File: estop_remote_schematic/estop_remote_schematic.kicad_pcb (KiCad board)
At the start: 2 copper layers, 60 x 75 mm, 22 parts, among them J1 Power Switch, J2 ESP32 Pins 1-22, J3 ESP32 Pins 23-44, J4 Battery Connector, J5 EStop Button, J6 OLed Screen Pins, J7 HC12 Connections, J8 Reset Button, J9 RotaryEnc Connections

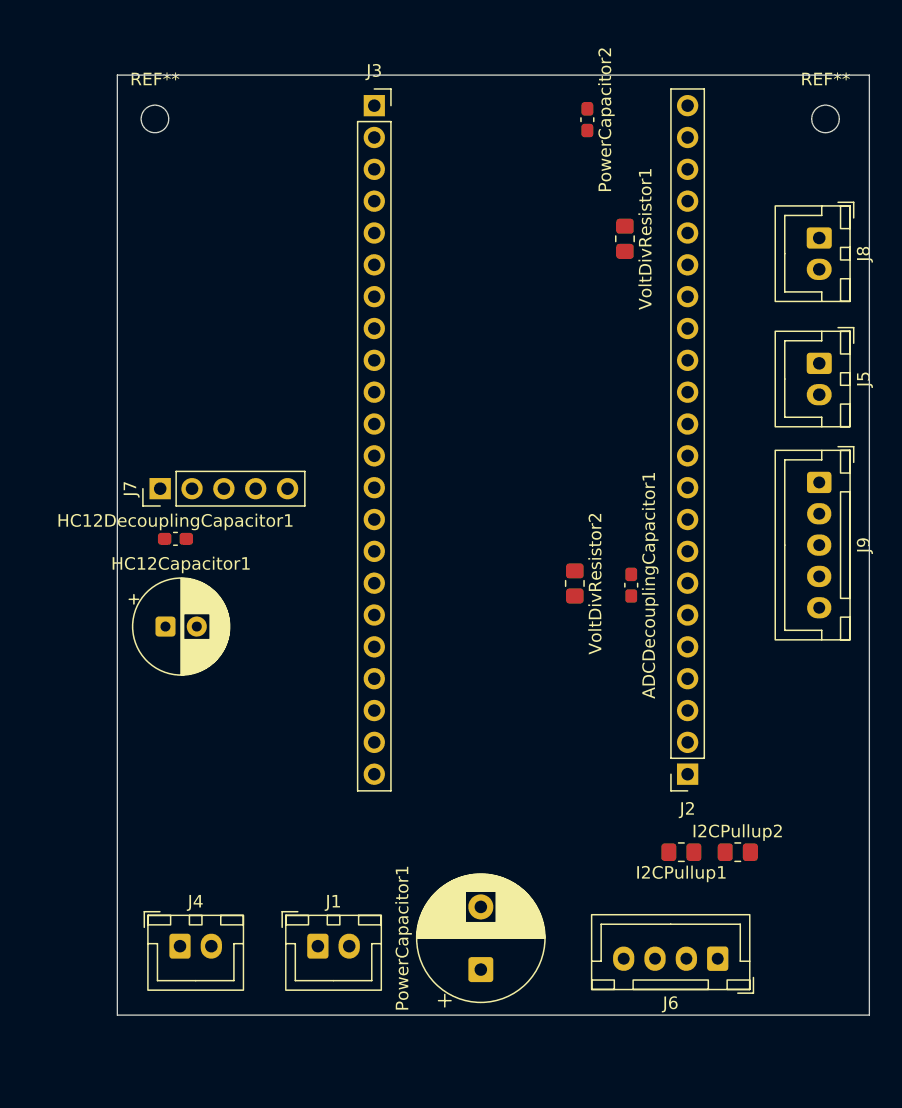
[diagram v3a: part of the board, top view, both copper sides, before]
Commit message: Added preliminary traces; connected all components and is ready for rule checks and ground plane
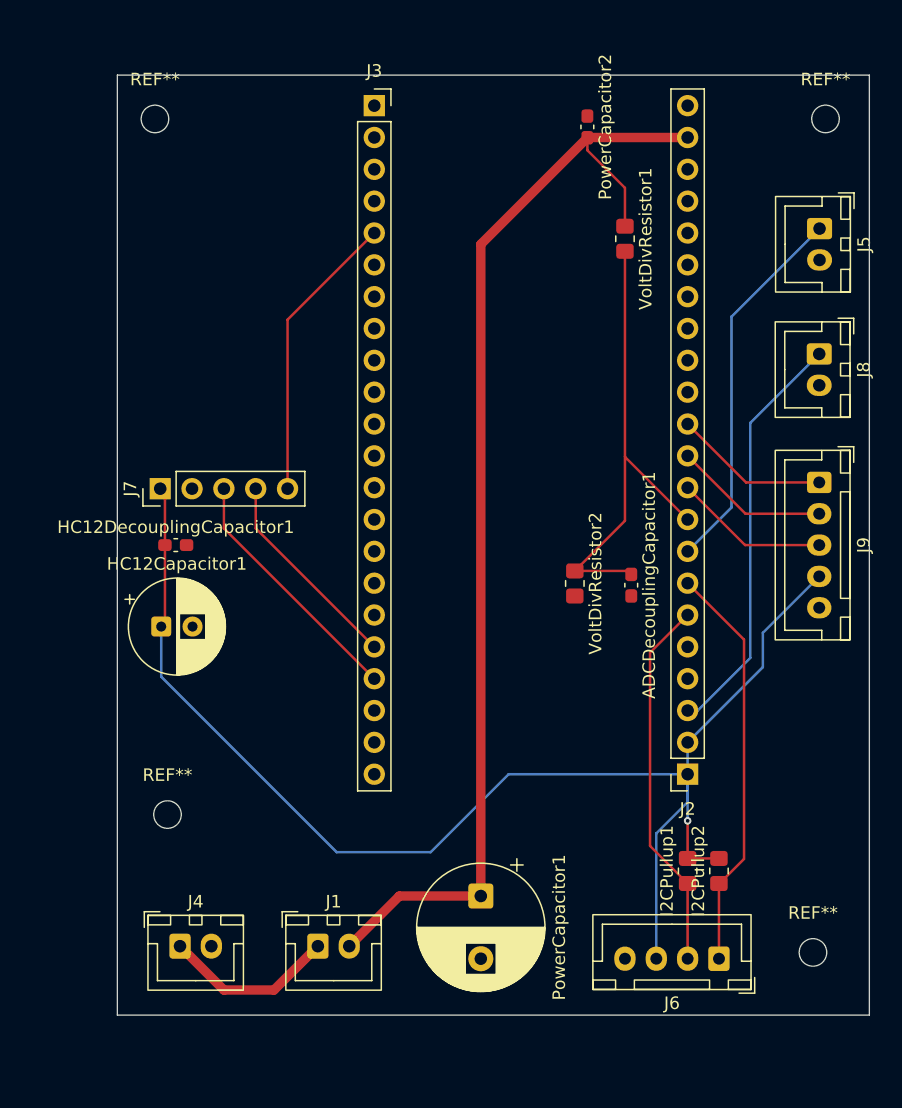
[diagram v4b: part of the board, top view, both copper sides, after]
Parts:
- added REF**: MountingHole_2.2mm_M2, MountingHole:MountingHole_2.2mm_M2, F.Cu at (123.5, 102.0)
- added REF**: MountingHole_2.2mm_M2, MountingHole:MountingHole_2.2mm_M2, F.Cu at (72.0, 91.0)
- moved J5 10.8 mm to (124.0, 44.2)
- moved J8 9.25 mm to (124.0, 54.2)
- moved PowerCapacitor1 5.87 mm to (97.0, 97.5), turned to -90 degrees
- moved I2CPullup2 2.12 mm to (116.0, 95.5), turned to 90 degrees
- moved I2CPullup1 1.58 mm to (113.5, 95.5), turned to 90 degrees
- moved PowerCapacitor2 0.58 mm to (105.5, 36.1)
- moved HC12DecouplingCapacitor1 0.50 mm to (72.7, 69.5)
- moved HC12Capacitor1 0.34 mm to (71.5, 76.0)
- moved J6 0.10 mm to (116.0, 102.5)
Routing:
- net +3.3V: track 0.00 -> 110.8 mm, vias 0 -> 1
- net +6V: track 0.00 -> 92.5 mm
- net /BatteryVoltageDivider: track 0.00 -> 38.8 mm
- net /Reset: track 0.00 -> 33.3 mm
- net /SDA: track 0.00 -> 32.7 mm
- net /EStopSignal: track 0.00 -> 30.1 mm
- net /SCL: track 0.00 -> 29.9 mm
- net /HC12_SET: track 0.00 -> 23.3 mm
- net /HC12_RX: track 0.00 -> 20.1 mm
- net /HC12_TX: track 0.00 -> 16.5 mm
- net Net-(J1-Pin_1): track 0.00 -> 13.9 mm
- net /ChannelEncoderB: track 0.00 -> 12.4 mm
- net /ChannelEncoderA: track 0.00 -> 12.4 mm
- net /ChannelEncoderSignal: track 0.00 -> 12.4 mm

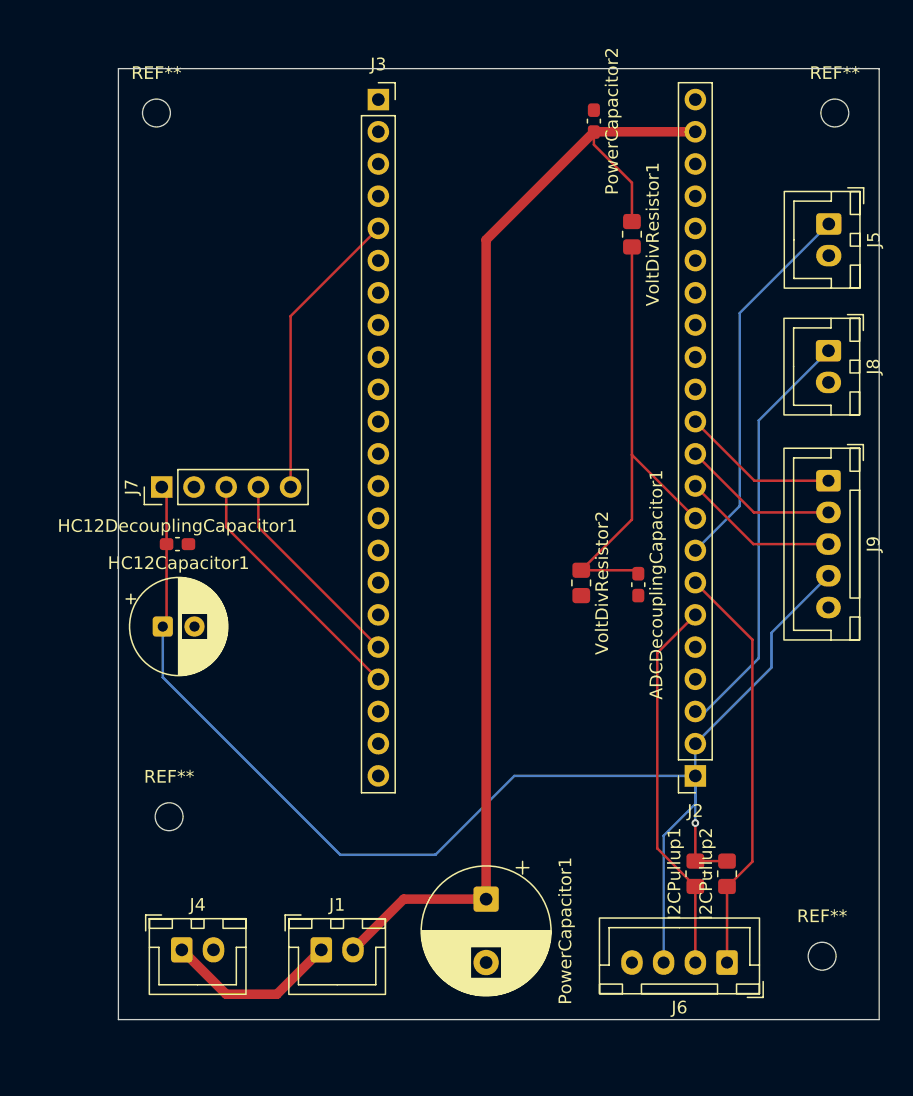
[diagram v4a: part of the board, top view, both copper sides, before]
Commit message: Poured ground plane on layer B.cu, added dog bone vias for SMT components
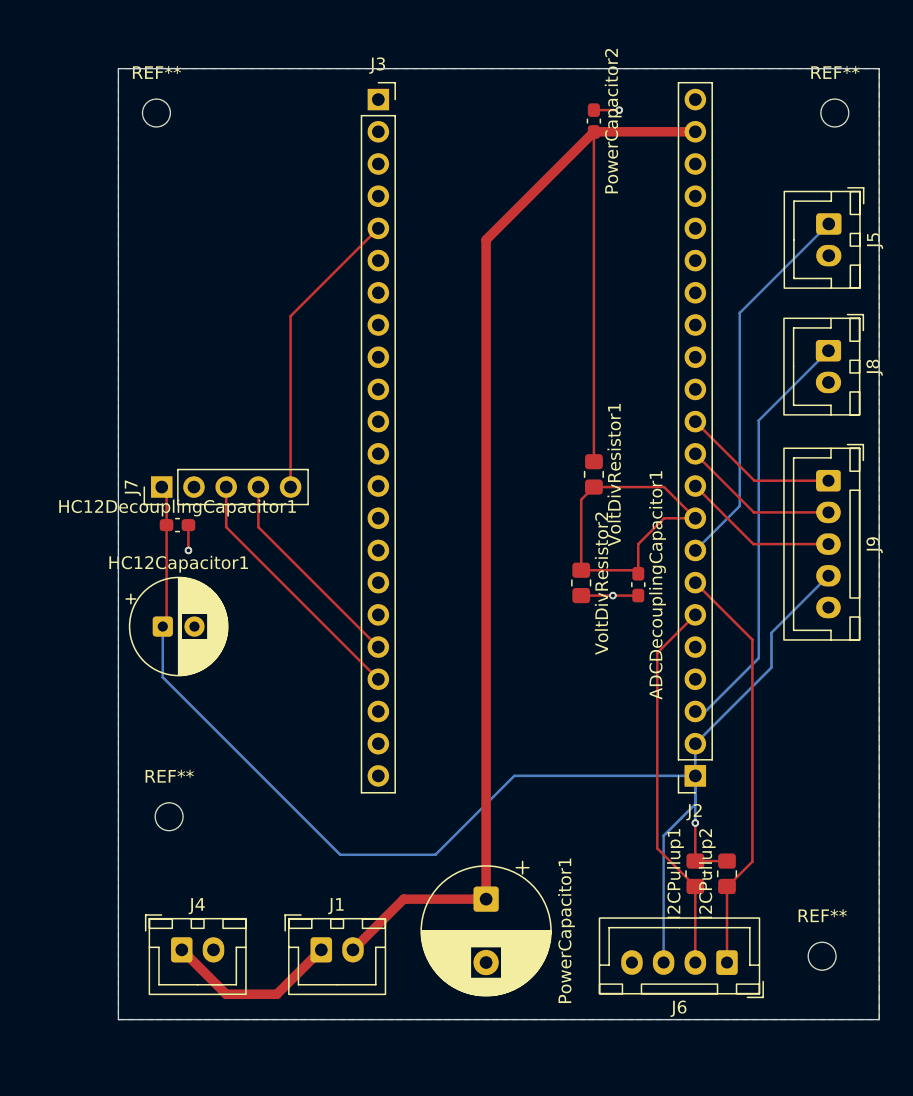
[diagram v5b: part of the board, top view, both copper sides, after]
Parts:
- moved VoltDivResistor1 19.2 mm to (105.5, 64.0)
- moved HC12DecouplingCapacitor1 1.50 mm to (72.7, 68.0)
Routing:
- net +6V: track 92.5 -> 110.2 mm
- net /BatteryVoltageDivider: track 38.8 -> 28.3 mm
- net GND: track 0.00 -> 8.50 mm, vias 0 -> 3
- added copper zone on B.Cu, net GND
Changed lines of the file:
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@@
 	(footprint "Resistor_SMD:R_0805_2012Metric_Pad1.20x1.40mm_HandSolder"
 		(layer "F.Cu")
-		(at 108.5 45.06 -90)
+		(at 105.5 64 -90)
 		(descr "Resistor SMD 0805 (2012 Metric), square (rectangular) end terminal, IPC-7351 nominal with elongated pad for handsoldering. (Body size source: IPC-SM-782 page 72, https://www.pcb-3d.com/wordpress/wp-content/uploads/ipc-sm-782a_amendment_1_and_2.pdf)")
 		(tags "resistor handsolder")
@@
 	(footprint "Capacitor_SMD:C_0603_1608Metric_Pad1.08x0.95mm_HandSolder"
 		(layer "F.Cu")
-		(at 72.661394 69.5)
+		(at 72.661394 68)
 		(descr "Capacitor SMD 0603 (1608 Metric), square (rectangular) end terminal, IPC-7351 nominal with elongated pad for handsoldering. (Body size source: IPC-SM-782 page 76, https://www.pcb-3d.com/wordpress/wp-content/uploads/ipc-sm-782a_amendment_1_and_2.pdf)")
 		(tags "capacitor handsolder")
@@
 	)
 	(segment
-		(start 97 97.5)
-		(end 90.5 97.5)
-		(width 0.75)
+		(start 104.5 73.56)
+		(end 107 73.56)
+		(width 0.2)
 		(layer "F.Cu")
-		(net "+6V")
+		(net "GND")
 	)
 	(segment
-		(start 105.5 38)
-		(end 108.5 41)
+		(start 73.523894 68)
+		(end 73.523894 70)
 		(width 0.2)
 		(layer "F.Cu")
+		(net "GND")
+	)
+	(segment
+		(start 107 73.56)
+		(end 109 73.56)
+		(width 0.2)
+		(layer "F.Cu")
+		(net "GND")
+	)
+	(segment
+		(start 105.5 35.275)
+		(end 107.5 35.275)
+		(width 0.2)
+		(layer "F.Cu")
+		(net "GND")
+	)
+	(via
+		(at 107.5 35.275)
+		(size 0.6)
+		(drill 0.3)
+		(layers "F.Cu" "B.Cu")
+		(net "GND")
+	)
+	(via
+		(at 73.523894 70)
+		(size 0.6)
+		(drill 0.3)
+		(layers "F.Cu" "B.Cu")
+		(net "GND")
+	)
+	(via
+		(at 107 73.56)
+		(size 0.6)
+		(drill 0.3)
+		(layers "F.Cu" "B.Cu")
+		(net "GND")
+	)
+	(segment
+		(start 97 97.5)
+		(end 90.5 97.5)
+		(width 0.75)
+		(layer "F.Cu")
 		(net "+6V")
 	)
@@
 	)
 	(segment
-		(start 113.5 36.98)
-		(end 105.52 36.98)
-		(width 0.75)
+		(start 105.5 37)
+		(end 105.5 63)
+		(width 0.2)
 		(layer "F.Cu")
 		(net "+6V")
 	)
 	(segment
-		(start 108.5 41)
-		(end 108.5 44.06)
-		(width 0.2)
+		(start 113.5 36.98)
+		(end 105.52 36.98)
+		(width 0.75)
 		(layer "F.Cu")
 		(net "+6V")
@@
 	)
 	(segment
-		(start 105.5 37)
-		(end 105.5 38)
+		(start 111.04 65)
+		(end 113.5 67.46)
 		(width 0.2)
 		(layer "F.Cu")
-		(net "+6V")
+		(net "/BatteryVoltageDivider")
+	)
+	(segment
+		(start 109 71.835)
+		(end 109 69.5)
+		(width 0.2)
+		(layer "F.Cu")
+		(net "/BatteryVoltageDivider")
 	)
 	(segment
@@
 	)
 	(segment
-		(start 108.5 67.56)
-		(end 104.5 71.56)
+		(start 105.5 65)
+		(end 111.04 65)
 		(width 0.2)
 		(layer "F.Cu")
@@
 	)
 	(segment
-		(start 108.5 46.06)
-		(end 108.5 62.46)
+		(start 111.04 67.46)
+		(end 113.5 67.46)
 		(width 0.2)
 		(layer "F.Cu")
@@
 	)
 	(segment
-		(start 108.725 71.56)
-		(end 109 71.835)
+		(start 104.5 66)
+		(end 104.5 71.56)
+		(width 0.2)
+		(layer "F.Cu")
+		(net "/BatteryVoltageDivider")
+	)
+	(segment
+		(start 109 69.5)
+		(end 111.04 67.46)
 		(width 0.2)
 		(layer "F.Cu")
@@
 	)
 	(segment
-		(start 113.5 67.46)
-		(end 108.5 62.46)
+		(start 108.725 71.56)
+		(end 109 71.835)
 		(width 0.2)
 		(layer "F.Cu")
@@
 	)
 	(segment
-		(start 108.5 62.46)
-		(end 108.5 67.56)
+		(start 105.5 65)
+		(end 104.5 66)
 		(width 0.2)
 		(layer "F.Cu")
@@
 	)
 	(segment
-		(start 71.798894 65.378894)
-		(end 71.42 65)
+		(start 71.798894 68)
+		(end 71.798894 75.701106)
 		(width 0.2)
 		(layer "F.Cu")
@@
 	)
 	(segment
-		(start 71.798894 69.5)
-		(end 71.798894 75.701106)
+		(start 71.798894 68)
+		(end 71.798894 65.378894)
 		(width 0.2)
 		(layer "F.Cu")
@@
 	)
 	(segment
-		(start 113.5 91.5)
-		(end 113.5 94.5)
+		(start 71.798894 75.701106)
+		(end 71.5 76)
 		(width 0.2)
 		(layer "F.Cu")
@@
 	)
 	(segment
-		(start 116 94.5)
+		(start 113.5 91.5)
 		(end 113.5 94.5)
 		(width 0.2)
@@
 	)
 	(segment
-		(start 71.798894 75.701106)
-		(end 71.5 76)
+		(start 116 94.5)
+		(end 113.5 94.5)
 		(width 0.2)
 		(layer "F.Cu")
@@
 	)
 	(segment
-		(start 71.798894 69.5)
-		(end 71.798894 65.378894)
+		(start 71.798894 65.378894)
+		(end 71.42 65)
 		(width 0.2)
 		(layer "F.Cu")
@@
 		(net "/SDA")
 	)
+	(zone
+		(net "GND")
+		(layer "B.Cu")
+		(hatch edge 0.5)
+		(connect_pads
+			(clearance 0.5)
+		)
+		(min_thickness 0.25)
+		(fill yes
+			(thermal_gap 0.5)
+			(thermal_bridge_width 0.5)
+			(island_removal_mode 0)
+		)
+		(polygon
+			(pts
+				(xy 128 32) (xy 68 32) (xy 68 107) (xy 128 107)
+			)
+		)
+	)
 	(embedded_fonts no)

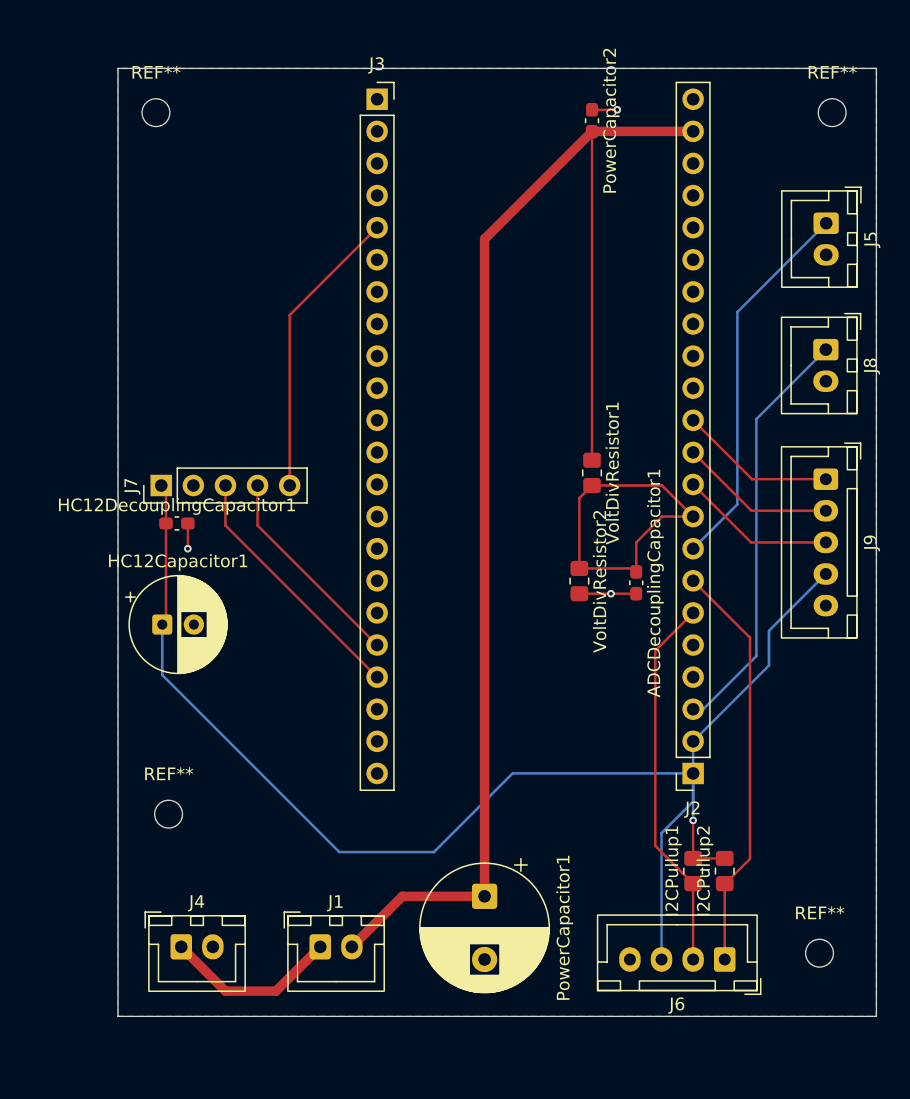
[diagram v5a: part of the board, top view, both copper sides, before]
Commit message: updated placements of SMD components to be more optimized for decoupling
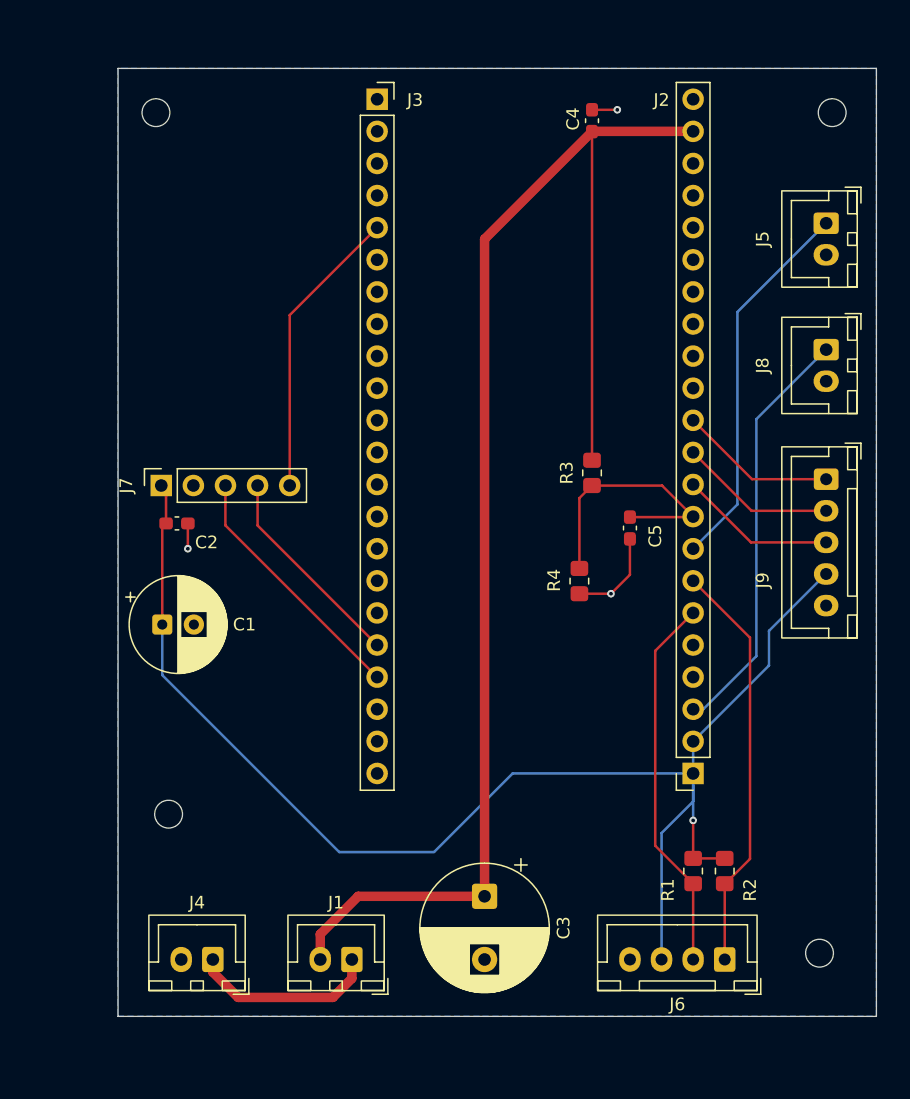
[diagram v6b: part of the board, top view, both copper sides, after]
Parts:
- J7: footprint Connector_PinHeader_2.54mm:PinHeader_1x05_P2.54mm_Vertical -> Connector_PinSocket_2.54mm:PinSocket_1x05_P2.54mm_Vertical
- moved C5 4.36 mm to (108.5, 68.4)
- moved J1 2.69 mm to (86.5, 102.5), turned to 180 degrees
- moved J4 2.69 mm to (75.5, 102.5), turned to 180 degrees
- renumbered HC12Capacitor1 to C1, HC12DecouplingCapacitor1 to C2, PowerCapacitor1 to C3, PowerCapacitor2 to C4, ADCDecouplingCapacitor1 to C5, I2CPullup1 to R1, I2CPullup2 to R2, VoltDivResistor1 to R3, VoltDivResistor2 to R4
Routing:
- net /BatteryVoltageDivider: track 28.3 -> 21.0 mm
- net +6V: track 110.2 -> 114.3 mm
- net GND: track 8.50 -> 11.5 mm
- net Net-(J1-Pin_1): track 13.9 -> 14.9 mm
